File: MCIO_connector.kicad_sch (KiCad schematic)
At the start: 1 part, among them J3 G97R24312HR_EP

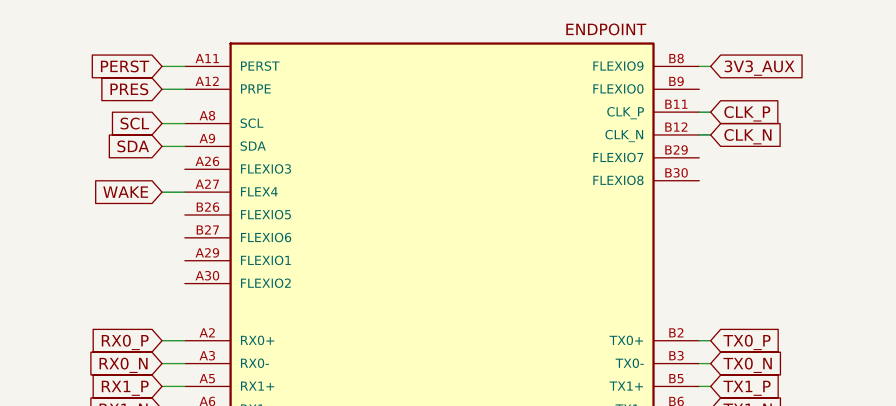
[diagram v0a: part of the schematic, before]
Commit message: updated stackup and regulator
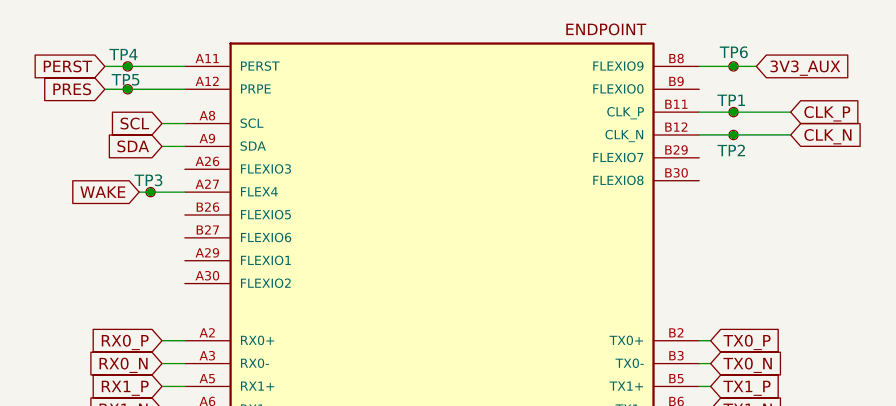
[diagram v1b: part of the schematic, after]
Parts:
- added TP1: CLK_P, TestPoint:TestPoint_Pad_D1.0mm, symbol Connector:TestPoint_Small
- added TP2: CLK_N, TestPoint:TestPoint_Pad_D1.0mm, symbol Connector:TestPoint_Small
- added TP3: WAKE, TestPoint:TestPoint_Pad_D1.0mm, symbol Connector:TestPoint_Small
- added TP4: PERST, TestPoint:TestPoint_Pad_D1.0mm, symbol Connector:TestPoint_Small
- added TP5: PRES, TestPoint:TestPoint_Pad_D1.0mm, symbol Connector:TestPoint_Small
- added TP6: 3V3_AUX, TestPoint:TestPoint_Pad_D1.0mm, symbol Connector:TestPoint_Small
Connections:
- net 3V3_AUX: now also TP6.1
- net CLK_N: now also TP2.1
- net CLK_P: now also TP1.1
- net PERST: now also TP4.1
- net PRES: now also TP5.1
- net WAKE: now also TP3.1
